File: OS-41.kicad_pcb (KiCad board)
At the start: 4 copper layers, 65 parts, among them J1 Conn_02x03_Counter_Clockwise, J2 Conn_01x02_Pin, J3 Conn_01x02_Pin, J4 Conn_Coaxial, SW4 SW_Push, U1 BME280, U2 SI4432-B1-FMR, U3 MCP1640x-xCHY, U4 ATGM336H-5N31, U7 STM32F103C8Tx, Y1 32.768KHz 12.5pF, Y2 8MHz 12pF, Y3 30MHz 10pF

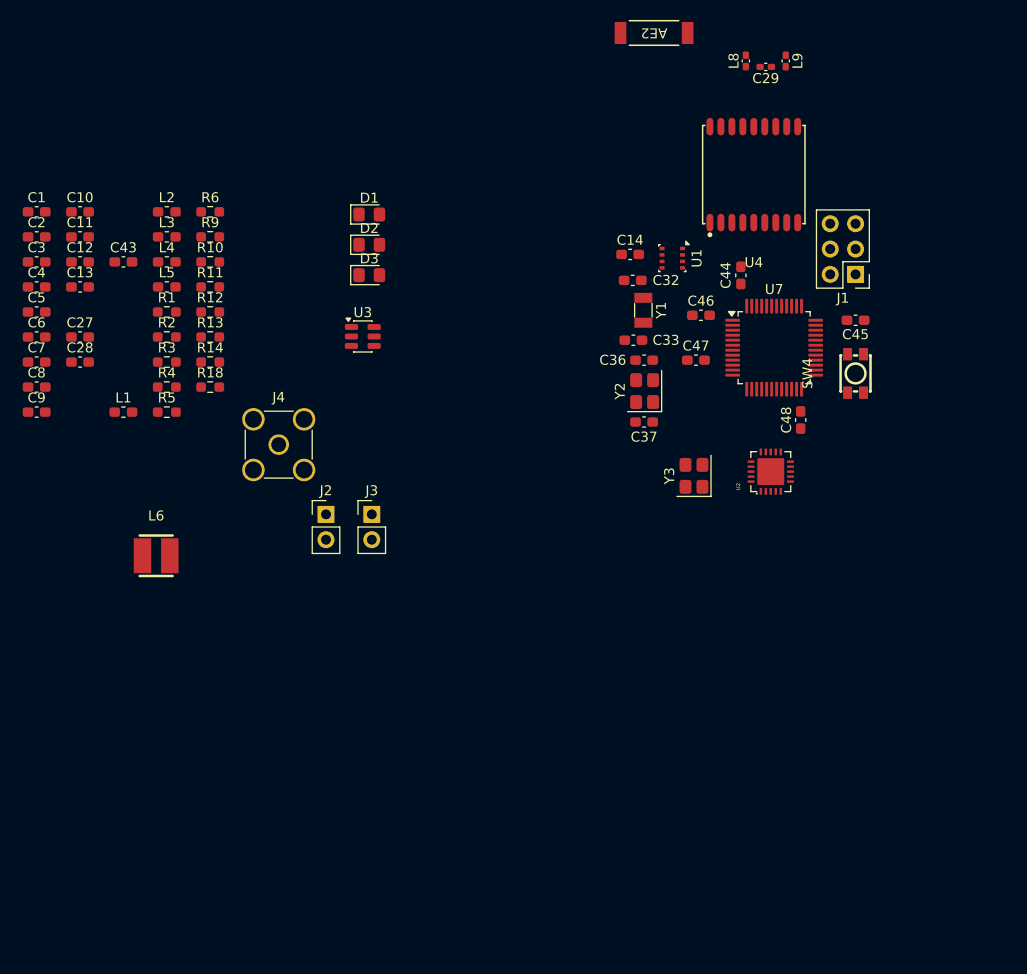
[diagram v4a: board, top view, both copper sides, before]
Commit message: More layout, no routing yet...
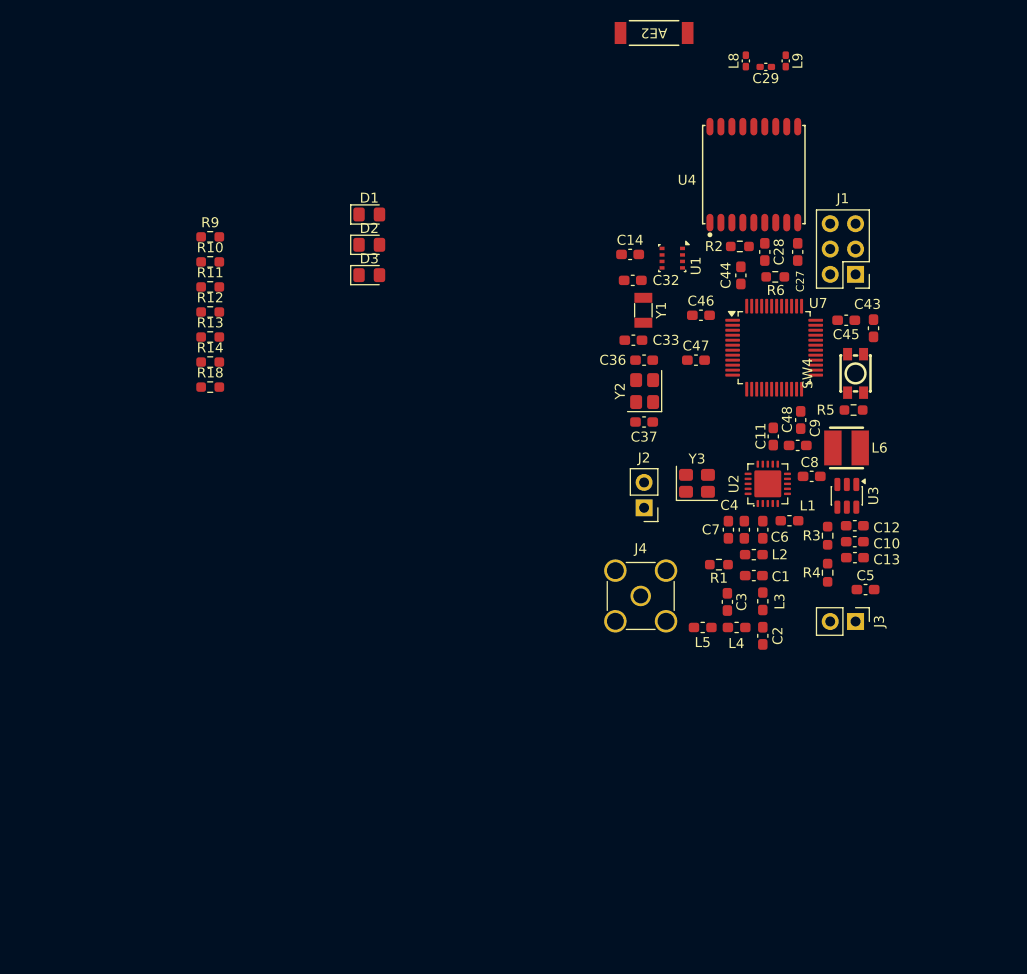
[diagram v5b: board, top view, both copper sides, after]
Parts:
- C11, C28: value 10uF -> 100nF
- R1: value 50 -> 50R
- moved C5 87.6 mm to (155.0, 107.0), turned to 180 degrees
- moved C10 84.4 mm to (153.9, 102.2)
- moved C2 83.1 mm to (144.7, 111.6), turned to 90 degrees
- moved C13 82.3 mm to (153.9, 103.8)
- moved C12 82.1 mm to (153.9, 100.6)
- moved C1 80.6 mm to (143.8, 105.6)
- moved C8 78.2 mm to (149.6, 95.7)
- moved C3 77.2 mm to (141.2, 108.2), turned to -90 degrees
- moved C9 76.4 mm to (148.2, 92.5)
- moved C43 75.5 mm to (155.8, 80.8), turned to 90 degrees
- moved C6 75.3 mm to (144.7, 101.0), turned to -90 degrees
- moved C4 75.0 mm to (142.8, 101.0), turned to -90 degrees
- moved C27 72.5 mm to (148.2, 73.2), turned to -90 degrees
- moved C11 72.3 mm to (145.8, 91.7), turned to 90 degrees
- moved C7 71.4 mm to (141.2, 101.0), turned to -90 degrees
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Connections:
- R5 pad 1: VCC_3.3 -> VCC

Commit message: Finished V1 layout!
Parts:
- moved R18 51.6 mm to (139.0, 72.8), turned to 180 degrees
- moved R13 48.3 mm to (136.2, 70.2), turned to -90 degrees
- moved R12 48.2 mm to (135.8, 66.5), turned to -90 degrees
- moved R14 47.0 mm to (136.0, 78.5), turned to -90 degrees
- moved R9 45.3 mm to (134.6, 70.3), turned to 90 degrees
- moved R11 44.4 mm to (132.5, 66.6), turned to -90 degrees
- moved R10 40.6 mm to (129.2, 66.6), turned to 90 degrees
- moved D3 33.1 mm to (135.8, 62.7), turned to -90 degrees
- moved D2 28.9 mm to (132.5, 62.7), turned to -90 degrees
- moved D1 24.8 mm to (129.2, 62.7), turned to -90 degrees
- moved AE2 3.91 mm to (132.7, 55.0)
- moved C29 2.65 mm to (145.1, 57.2)
- moved L8 2.65 mm to (143.1, 56.6)
- moved L9 2.65 mm to (147.1, 56.6)

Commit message: Layout initial done
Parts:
- moved J2 3.09 mm to (129.8, 98.3)
- moved J1 1.87 mm to (155.6, 74.4)
- moved C47 1.77 mm to (139.0, 85.5), turned to 90 degrees
- moved AE2 0.74 mm to (132.0, 55.2)
- moved J3 0.55 mm to (154.0, 110.8)
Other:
- board outline added: 32.5 x 61 mm
- board text added: "CLK"
- board text added: "DIO"
- board text added: "GND"
- board text added: "GPS"
- board text added: "MCU"
- board text added: "OS-41"
- board text added: "PROG"
- board text added: "RESET"
- board text added: "RF"
- board text added: "RF OUT"
- board text added: "RST"
- board text added: "Rev. E"
- board text added: "VCC"

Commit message: Start routing!
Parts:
- moved R14 5.59 mm to (131.4, 75.3), turned to 180 degrees
- moved C37 4.45 mm to (137.1, 89.0)
- moved C36 4.40 mm to (137.1, 83.0)
- moved Y2 4.38 mm to (137.1, 86.0)
- moved C32 4.18 mm to (135.7, 77.2)
- moved Y1 3.95 mm to (136.6, 80.0)
- moved C47 2.56 mm to (140.2, 87.8)
- moved C33 2.01 mm to (133.6, 81.3)
- moved C46 1.71 mm to (139.7, 78.2), turned to -90 degrees
- moved Y3 0.90 mm to (138.9, 96.0)
- moved C5 0.20 mm to (155.0, 106.8)
- turned R10 to -90 degrees
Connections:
- C43 pad 2: unconnected-(C43-Pad2) -> GND
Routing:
- net VCC: track 0.00 -> 36.1 mm, vias 0 -> 10
- net RST: track 0.00 -> 31.5 mm, vias 0 -> 2
- net GND: track 0.00 -> 30.9 mm, vias 0 -> 42
- net NIRQ: track 0.00 -> 21.2 mm, vias 0 -> 2
- net TXD: track 0.00 -> 21.0 mm, vias 0 -> 2
- net RXD: track 0.00 -> 17.4 mm, vias 0 -> 2
- net BATT: track 0.00 -> 16.9 mm, vias 0 -> 2
- net Net-(AE2-A): track 0.00 -> 10.0 mm
- net SYS_JTMS-SWDIO: track 0.00 -> 9.33 mm
- net X_OUT: track 0.00 -> 8.87 mm
- net NSEL: track 0.00 -> 8.74 mm
- net X_IN: track 0.00 -> 8.74 mm
- net SDO: track 0.00 -> 8.19 mm, vias 0 -> 2
- net SCLK: track 0.00 -> 8.05 mm
- net SDI: track 0.00 -> 7.83 mm
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- added copper zone on B.Cu, net GND
- added copper zone on F.Cu, net GND
- added copper zone on In1.Cu, net GND
- added copper zone on In2.Cu, net VCC
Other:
- board text added: "+"
- board text added: "-"
- board text added: "ERR"
- board text added: "OK"
- board text added: "ON"
- board text added: "PWR IN"
- board text added: "PWR OUT"
